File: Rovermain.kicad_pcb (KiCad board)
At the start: 2 copper layers, 59 parts, among them J1 48V input, J10 3V3 Output, J11 5V Output, J13 Steering Bus Bar, J14 Drive Bus Bar, J15 Arm Bus Bar, J16 Pi_48V_Ctrl, J17 Spare 48V port, J2 USB_C_Receptacle_Pi_Power, J3 24V Output, J4 USB_C_Receptacle_Spare_power, J5 Buck 48/24, J6 Buck 24/12, J7 Buck 24/5, J8 Buck 12/3v3, J9 12V Output, Q1 Arm ctrl, Q2 Steer ctrl, Q3 Drive ctrl, Q4 Spare ctrl, SW2 SW_Push_Open

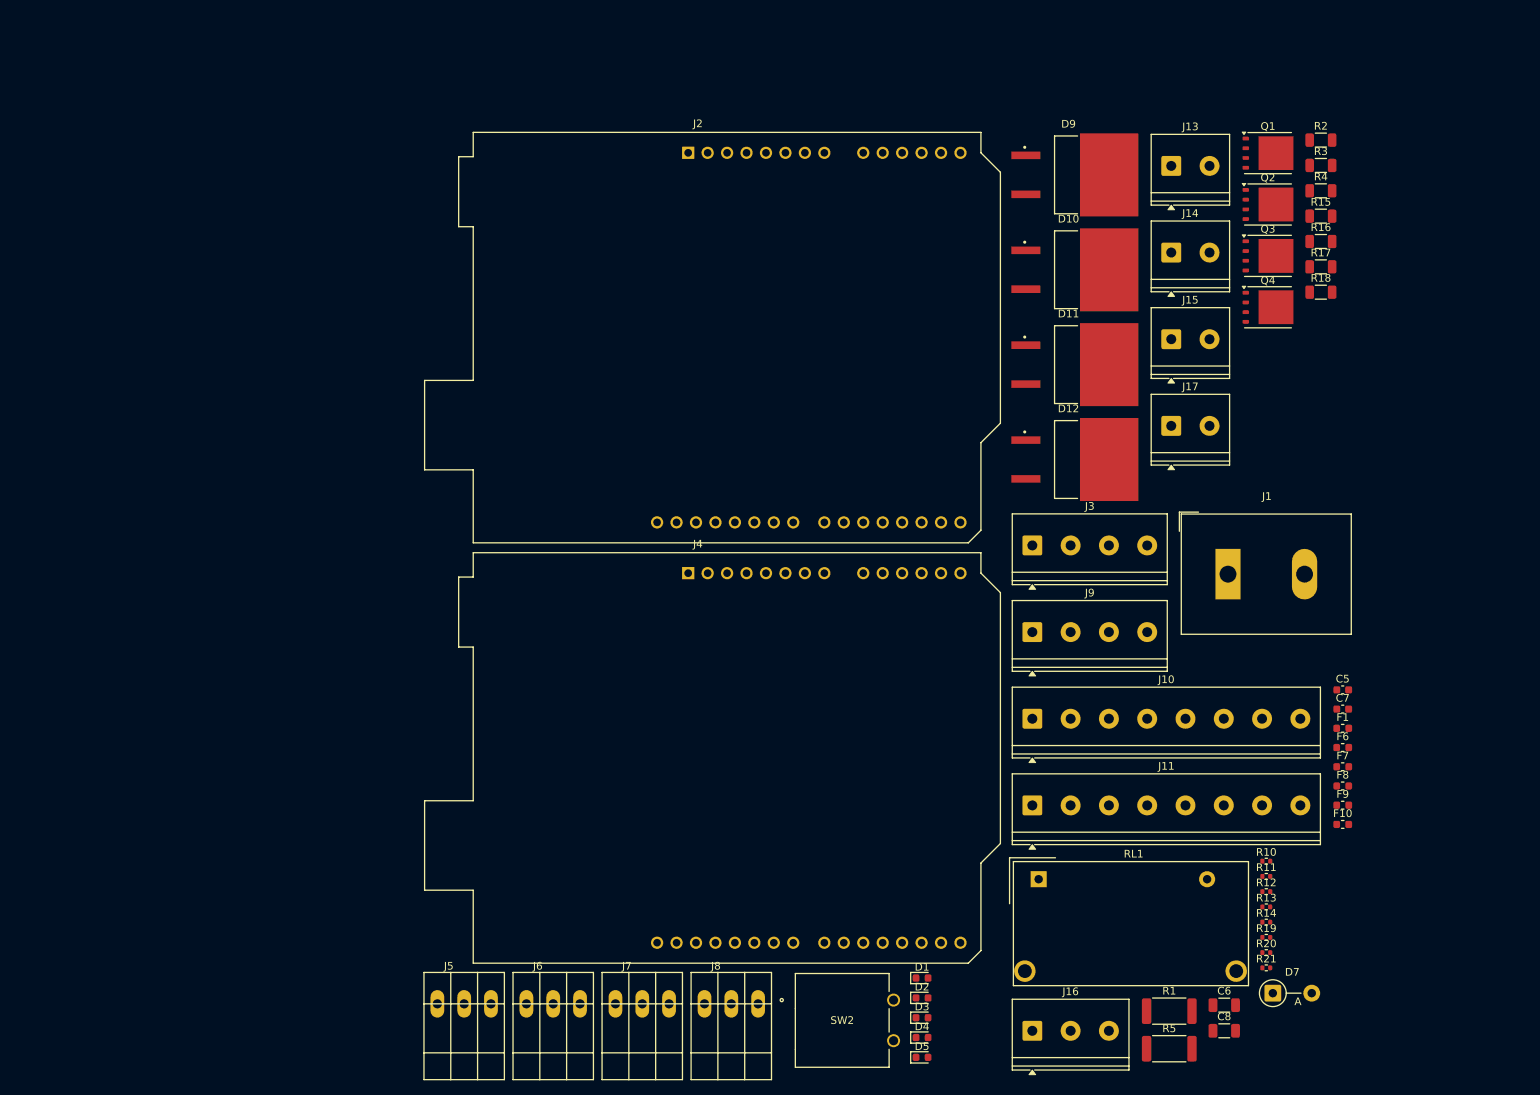
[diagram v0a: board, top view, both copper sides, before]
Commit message: updated footprints
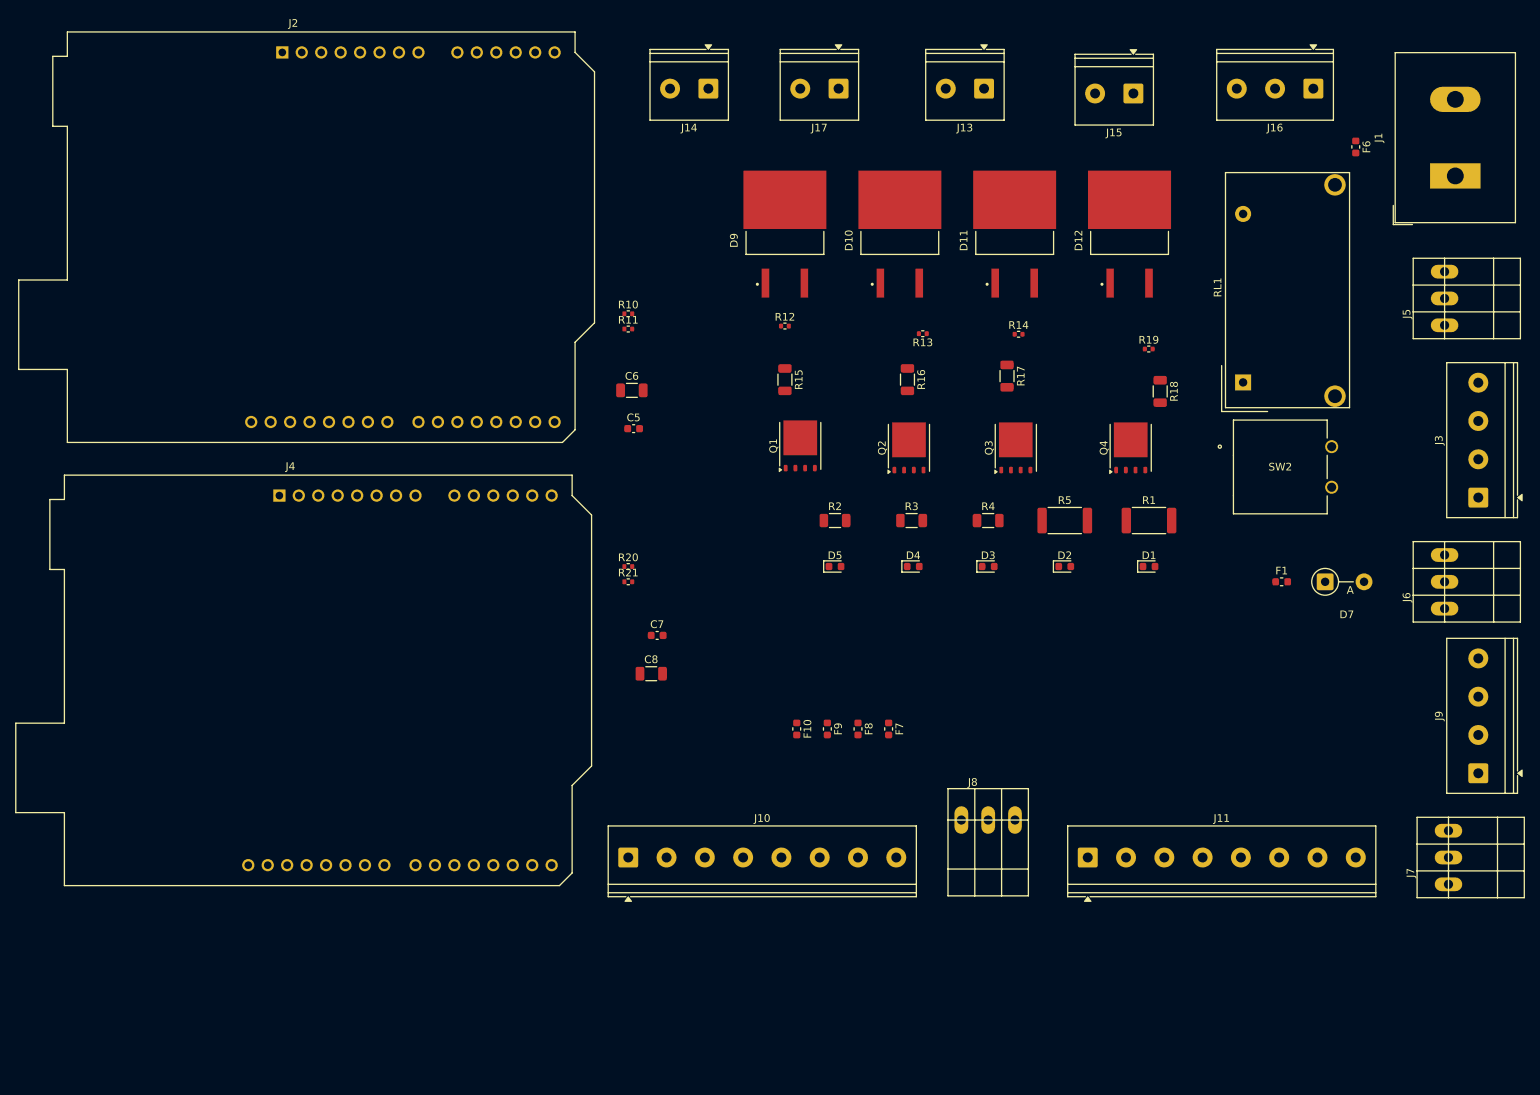
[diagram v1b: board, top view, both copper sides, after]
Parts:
- moved J5 166.7 mm to (225.0, 50.0), turned to 90 degrees
- moved J6 137.3 mm to (225.0, 87.0), turned to 90 degrees
- moved J16 128.4 mm to (201.5, 22.6), turned to 180 degrees
- moved J7 114.6 mm to (225.5, 123.0), turned to 90 degrees
- moved C6 111.5 mm to (112.5, 62.0)
- moved R10 109.8 mm to (112.0, 52.0)
- moved R11 109.8 mm to (112.0, 54.0)
- moved C5 98.7 mm to (112.7, 67.0)
- moved R20 97.4 mm to (112.0, 85.0)
- moved R21 97.4 mm to (112.0, 87.0)
- moved R12 97.0 mm to (132.5, 53.6)
- moved SW2 92.2 mm to (203.9, 69.3)
- moved C7 90.0 mm to (115.8, 94.0)
- moved C8 88.2 mm to (115.0, 99.0)
- moved R13 87.3 mm to (150.5, 54.6), turned to 180 degrees
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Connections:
- C6 pad 1: +3v3 -> /+3v3
- C8 pad 1: +3v3 -> /+3v3
- D10 pad 1: 48V -> /+3v3
- D11 pad 1: 48V -> /+3v3
- D12 pad 1: 48V -> /+3v3
- D2 pad 2: +3v3 -> /+3v3
- D3 pad 2: +3v3 -> /+3v3
- D4 pad 2: +3v3 -> /+3v3
- D5 pad 2: +3v3 -> /+3v3
- D9 pad 1: 48V -> /+3v3
- F1 pad 1: +3v3 -> /+3v3
- F10 pad 1: +3v3 -> /+3v3
- F7 pad 2: +3v3 -> /+3v3
- F8 pad 2: +3v3 -> /+3v3
- F9 pad 2: +3v3 -> /+3v3
- J10 pad 2: +3v3 -> /+3v3
- J10 pad 4: +3v3 -> /+3v3
- J10 pad 6: +3v3 -> /+3v3
- J10 pad 8: +3v3 -> /+3v3
- J11 pad 2: +3v3 -> /+3v3
- J11 pad 4: +3v3 -> /+3v3
- J11 pad 6: +3v3 -> /+3v3
- J11 pad 8: +3v3 -> /+3v3
- J3 pad 2: +3v3 -> /+3v3
- J3 pad 4: +3v3 -> /+3v3
- J5 pad 3: +3v3 -> /+3v3
- J6 pad 3: +3v3 -> /+3v3
- J7 pad 3: +3v3 -> /+3v3
- J8 pad 3: +3v3 -> /+3v3
- J9 pad 2: +3v3 -> /+3v3
- J9 pad 4: +3v3 -> /+3v3
- R1 pad 1: +3v3 -> /+3v3
- RL1 pad 13: +3v3 -> /+3v3

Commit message: Routing part 1
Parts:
- removed J16: Pi_48V_Ctrl, TerminalBlock_Phoenix:TerminalBlock_Phoenix_PT-1,5-3-5.0-H_1x03_P5.00mm_Horizontal
- added J12: Pi_48V_Control, TerminalBlock_Phoenix:TerminalBlock_Phoenix_PT-1,5-4-5.0-H_1x04_P5.00mm_Horizontal, F.Cu at (181.0, 22.0)
- J5, J6, J7: footprint Phoenix-3PT-1984028:1984028 -> TerminalBlock_Phoenix:TerminalBlock_Phoenix_PT-1,5-3-5.0-H_1x03_P5.00mm_Horizontal
- J8: value Buck 12/3v3 -> Buck 12/3V3; footprint Phoenix-3PT-1984028:1984028 -> TerminalBlock_Phoenix:TerminalBlock_Phoenix_PT-1,5-3-5.0-H_1x03_P5.00mm_Horizontal
- moved F7 97.4 mm to (210.0, 32.8)
- moved R5 77.5 mm to (218.0, 19.0)
- moved F8 74.8 mm to (210.0, 75.0)
- moved D2 70.2 mm to (210.0, 28.0), turned to -90 degrees
- moved F9 70.1 mm to (208.0, 109.2)
- moved R18 67.7 mm to (118.0, 38.4)
- moved R19 66.3 mm to (118.0, 32.9)
- moved Q4 64.2 mm to (116.8, 48.8)
- moved D4 61.6 mm to (203.0, 115.0)
- moved R3 57.9 mm to (198.5, 109.0)
- moved D3 53.2 mm to (210.0, 70.0), turned to -90 degrees
- moved R4 53.0 mm to (210.0, 64.5), turned to 90 degrees
- moved D11 45.3 mm to (124.0, 65.5)
- moved R1 40.3 mm to (185.0, 39.0), turned to -90 degrees
- moved D1 38.3 mm to (185.0, 47.0), turned to 90 degrees
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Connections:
- C6 pad 1: /+3v3 -> /+5V
- C8 pad 1: /+3v3 -> /+5V
- D10 pad 1: /+3v3 -> /48V
- D10 pad 3: (no net) -> /48V
- D10 pad 4: (no net) -> Net-(D10-A)
- D11 pad 1: /+3v3 -> /48V
- D11 pad 3: (no net) -> /48V
- D11 pad 4: (no net) -> Net-(D11-A)
- D12 pad 1: /+3v3 -> /48V
- D12 pad 3: (no net) -> /48V
- D12 pad 4: (no net) -> Net-(D12-A)
- D2 pad 2: /+3v3 -> /24V
- D3 pad 2: /+3v3 -> /12V
- D4 pad 2: /+3v3 -> /+5V
- D9 pad 1: /+3v3 -> /48V
- D9 pad 3: (no net) -> /48V
- D9 pad 4: (no net) -> Net-(D9-A)
- F1 pad 1: /+3v3 -> /+5V
- F10 pad 2: /Vout -> Net-(J8-Pin_1)
- F6 pad 1: /+ -> Net-(J1-Pin_2)
- F7 pad 1: /Vout -> Net-(J5-Pin_1)
- F7 pad 2: /+3v3 -> /24V
- F8 pad 1: /Vout -> Net-(J6-Pin_1)
- F8 pad 2: /+3v3 -> /12V
- F9 pad 1: /Vout -> Net-(J7-Pin_1)
- F9 pad 2: /+3v3 -> /+5V
- J1 pad 2: /+ -> Net-(J1-Pin_2)
- J11 pad 2: /+3v3 -> /+5V
- J11 pad 4: /+3v3 -> /+5V
- J11 pad 6: /+3v3 -> /+5V
- J11 pad 8: /+3v3 -> /+5V
- J13 pad 1: /+ -> Net-(D9-A)
- J13 pad 2: GNDREF -> Net-(J13-Pin_2)
- J14 pad 1: /+ -> Net-(D10-A)
- J14 pad 2: GNDREF -> Net-(J14-Pin_2)
- J15 pad 1: GNDREF -> Net-(J15-Pin_1)
- J15 pad 2: /+ -> Net-(D12-A)
- J17 pad 1: /+ -> Net-(D11-A)
- J17 pad 2: GNDREF -> Net-(J17-Pin_2)
- J3 pad 2: /+3v3 -> /24V
- J3 pad 4: /+3v3 -> /24V
- J5 pad 1: /Vout -> Net-(J5-Pin_1)
- J5 pad 3: /+3v3 -> /48V
- J6 pad 1: /Vout -> Net-(J6-Pin_1)
- J6 pad 3: /+3v3 -> /24V
- J7 pad 1: /Vout -> Net-(J7-Pin_1)
- J7 pad 3: /+3v3 -> /24V
- J8 pad 1: /Vout -> Net-(J8-Pin_1)
- J8 pad 3: /+3v3 -> /12V
- J9 pad 2: /+3v3 -> /12V
- J9 pad 4: /+3v3 -> /12V
- Q1 pad 4: /G -> Net-(Q1-G)
- Q1 pad 5: GNDREF -> Net-(J15-Pin_1)
- Q2 pad 4: /G -> Net-(Q2-G)
- Q2 pad 5: GNDREF -> Net-(J13-Pin_2)
- Q3 pad 4: /G -> Net-(Q3-G)
- Q3 pad 5: GNDREF -> Net-(J14-Pin_2)
- Q4 pad 4: /G -> Net-(Q4-G)
- Q4 pad 5: GNDREF -> Net-(J17-Pin_2)
- R1 pad 1: /+3v3 -> /48V
- R13 pad 2: Net-(J16-Pin_3) -> Net-(J12-Pin_3)
- R15 pad 2: /G -> Net-(Q1-G)
- R16 pad 1: Net-(J16-Pin_3) -> Net-(J12-Pin_3)
- R16 pad 2: /G -> Net-(Q2-G)
- R17 pad 2: /G -> Net-(Q3-G)
- R18 pad 1: Net-(J16-Pin_3) -> Net-(J12-Pin_4)
- R18 pad 2: /G -> Net-(Q4-G)
- R19 pad 2: Net-(J16-Pin_3) -> Net-(J12-Pin_4)
- RL1 pad 13: /+3v3 -> /48V
- SW2 pad 6: (no net) -> Net-(SW2-B)
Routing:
- net /48V: track 0.00 -> 173.9 mm
- net /12V: track 0.00 -> 140.0 mm
- net /24V: track 0.00 -> 129.9 mm
- net /+5V: track 0.00 -> 99.8 mm
- net Net-(J12-Pin_4): track 0.00 -> 85.1 mm
- net Net-(J12-Pin_3): track 0.00 -> 65.0 mm
- net /+3v3: track 0.00 -> 60.1 mm
- net Net-(D12-A): track 0.00 -> 47.6 mm
- net Net-(J12-Pin_2): track 0.00 -> 45.7 mm
- net Net-(D10-A): track 0.00 -> 42.7 mm
- net Net-(D9-A): track 0.00 -> 42.3 mm
- net Net-(D11-A): track 0.00 -> 41.9 mm
- net Net-(J15-Pin_1): track 0.00 -> 29.8 mm
- net Net-(J17-Pin_2): track 0.00 -> 27.8 mm
- net Net-(J14-Pin_2): track 0.00 -> 27.5 mm
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
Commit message: Routed everything but GNDs
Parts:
- J2, J4: footprint Module:Arduino_UNO_R2 -> USB-C-PD-2171750001:2171750001_MOL
- moved J2 61.6 mm to (122.6, 44.0), turned to -90 degrees
- moved J4 59.3 mm to (122.6, 56.7), turned to -90 degrees
- moved J12 58.1 mm to (123.0, 19.0), turned to -90 degrees
- moved J10 54.6 mm to (123.2, 69.0), turned to -90 degrees
- moved C8 47.2 mm to (132.0, 55.0), turned to 180 degrees
- moved C7 40.8 mm to (127.7, 55.0), turned to -90 degrees
- moved C5 35.1 mm to (127.7, 42.0), turned to 90 degrees
- moved C6 33.4 mm to (132.0, 42.0), turned to 180 degrees
- moved D5 32.5 mm to (138.2, 93.0)
- moved R20 31.0 mm to (128.0, 58.5), turned to -90 degrees
- moved J7 30.6 mm to (197.0, 101.4), turned to 0 degrees
- moved R21 29.7 mm to (128.0, 62.0), turned to -90 degrees
- moved F10 28.9 mm to (133.2, 93.0)
- moved J8 28.1 mm to (133.9, 101.3)
- moved J11 27.4 mm to (153.0, 101.4)
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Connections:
- C5 pad 1: Net-(C5-Pad1) -> /+5V
- C5 pad 2: Net-(C5-Pad2) -> GNDREF
- C6 pad 1: /+5V -> GNDREF
- C6 pad 2: Net-(C5-Pad2) -> /+5V
- C7 pad 1: Net-(C7-Pad1) -> /+5V
- C7 pad 2: Net-(C7-Pad2) -> GNDREF
- C8 pad 1: /+5V -> GNDREF
- C8 pad 2: Net-(C7-Pad2) -> /+5V
- J12 pad 1: Net-(J12-Pin_4) -> Net-(J12-Pin_1)
- J12 pad 2: Net-(J12-Pin_3) -> Net-(J12-Pin_2)
- J12 pad 3: Net-(J12-Pin_2) -> Net-(J12-Pin_3)
- J12 pad 4: Net-(J12-Pin_1) -> Net-(J12-Pin_4)
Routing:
- net /+5V: track 99.8 -> 194.9 mm
- net Net-(J12-Pin_4): track 85.1 -> 37.5 mm
- net Net-(J12-Pin_1): track 26.4 -> 70.9 mm
- net /12V: track 140.0 -> 112.6 mm
- net Net-(J12-Pin_3): track 65.0 -> 46.4 mm
- net /24V: track 129.9 -> 114.1 mm
- net Net-(J12-Pin_2): track 45.7 -> 58.6 mm
- net Net-(J7-Pin_1): track 19.8 -> 9.32 mm
- net Net-(J2-CC1): track 0.00 -> 10.2 mm
- net Net-(J2-CC2): track 0.00 -> 7.35 mm
- net Net-(J4-CC2): track 0.00 -> 5.77 mm
- net /48V: track 173.9 -> 168.9 mm
- net /+3v3: track 60.1 -> 55.4 mm
- net Net-(D10-A): track 42.7 -> 39.5 mm
- net Net-(J4-CC1): track 0.00 -> 3.15 mm
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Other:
- board outline added: 4.4 x 8.6 mm

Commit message: more routing; added fuses
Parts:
- added F11: Fuse, Fuse:Fuse_0603_1608Metric, F.Cu at (143.5, 75.0)
- added F12: Fuse, Fuse:Fuse_0603_1608Metric, F.Cu at (158.5, 75.0)
- added F13: Fuse, Fuse:Fuse_0603_1608Metric, F.Cu at (173.5, 75.0)
- added F14: Fuse, Fuse:Fuse_0603_1608Metric, F.Cu at (186.8, 76.0)
- moved J2 5.34 mm to (121.0, 49.1)
- moved J4 5.34 mm to (121.0, 61.8)
- moved RL1 5.11 mm to (192.3, 66.1)
- moved C5 5.11 mm to (127.7, 47.1)
- moved C6 5.11 mm to (132.0, 47.1)
- moved C7 5.11 mm to (127.7, 60.1)
- moved C8 5.11 mm to (132.0, 60.1)
- moved D1 5.11 mm to (185.0, 52.1)
- moved D10 5.11 mm to (166.0, 70.6)
- moved D11 5.11 mm to (136.0, 70.6)
- moved D12 5.11 mm to (181.0, 70.6)
- moved D2 5.11 mm to (210.0, 33.1)
- moved D3 5.11 mm to (210.0, 75.1)
- moved D4 5.11 mm to (198.8, 98.1)
- moved D5 5.11 mm to (138.2, 98.1)
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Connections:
- D10 pad 1: /48V -> Net-(D10-K)
- D10 pad 3: /48V -> Net-(D10-K)
- D11 pad 1: /48V -> Net-(D11-K)
- D11 pad 3: /48V -> Net-(D11-K)
- D12 pad 1: /48V -> Net-(D12-K)
- D12 pad 3: /48V -> Net-(D12-K)
- D9 pad 1: /48V -> Net-(D9-K)
- D9 pad 3: /48V -> Net-(D9-K)
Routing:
- net GNDREF: track 0.00 -> 88.7 mm, vias 0 -> 18
- net /48V: track 168.9 -> 132.0 mm
- net Net-(D9-K): track 0.00 -> 15.1 mm
- net Net-(D11-K): track 0.00 -> 15.1 mm
- net Net-(D10-K): track 0.00 -> 15.1 mm
- net Net-(D12-K): track 0.00 -> 8.41 mm
- net /+5V: track 194.9 -> 199.6 mm
- net Net-(J2-CC2): track 7.35 -> 8.92 mm
- net Net-(J2-CC1): track 10.2 -> 11.7 mm
- net Net-(J4-CC1): track 3.15 -> 4.71 mm
- net Net-(J4-CC2): track 5.77 -> 7.33 mm
- added copper zone on B.Cu, net GNDREF
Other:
- board size 4.4 x 8.6 mm -> 120 x 105 mm

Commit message: updated usb-c ports; finalized routing
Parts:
- J2, J4: footprint USB-C-PD-2171750001:2171750001_MOL -> Real_USB-C-PD-2171750001:2171750001_MOL
- moved R10 9.76 mm to (127.0, 45.4)
- moved R20 4.71 mm to (127.0, 59.0)
- moved C5 2.39 mm to (127.0, 49.4)
- moved C6 2.19 mm to (130.0, 48.0), turned to -90 degrees
- moved C7 2.02 mm to (127.0, 62.0), turned to 90 degrees
- moved J4 1.57 mm to (122.0, 63.0)
- moved R21 1.49 mm to (127.0, 66.0)
- moved J2 1.34 mm to (122.0, 50.0)
- moved R11 1.34 mm to (127.0, 53.0)
- moved C8 1.00 mm to (131.0, 60.1)
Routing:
- net Net-(D12-K): track 8.41 -> 17.1 mm
- net Net-(D9-K): track 15.1 -> 21.5 mm
- net Net-(D10-K): track 15.1 -> 20.9 mm
- net Net-(D11-K): track 15.1 -> 20.4 mm
- net GNDREF: track 88.7 -> 84.2 mm, vias 18 -> 19
- net Net-(J4-CC1): track 4.71 -> 8.95 mm
- net Net-(J4-CC2): track 7.33 -> 11.4 mm
- net /+5V: track 199.6 -> 195.5 mm
- net Net-(J2-CC1): track 11.7 -> 8.70 mm
- net Net-(J2-CC2): track 8.92 -> 10.6 mm
